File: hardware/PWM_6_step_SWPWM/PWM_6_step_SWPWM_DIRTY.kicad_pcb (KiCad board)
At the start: 2 copper layers, 104.6 x 84.2 mm, 40 parts, among them J1 Conn_01x15, J2 Conn_01x15, J3 Screw_Terminal_01x02, J4 Conn_01x06_Pin, J5 Screw_Terminal_01x03, Q1 IRLZ44N, Q2 IRLZ44N, Q3 IRLZ44N, Q4 IRLZ44N, Q5 IRLZ44N, Q6 IRLZ44N, U1 IR2110, U2 IR2110, U3 IR2110

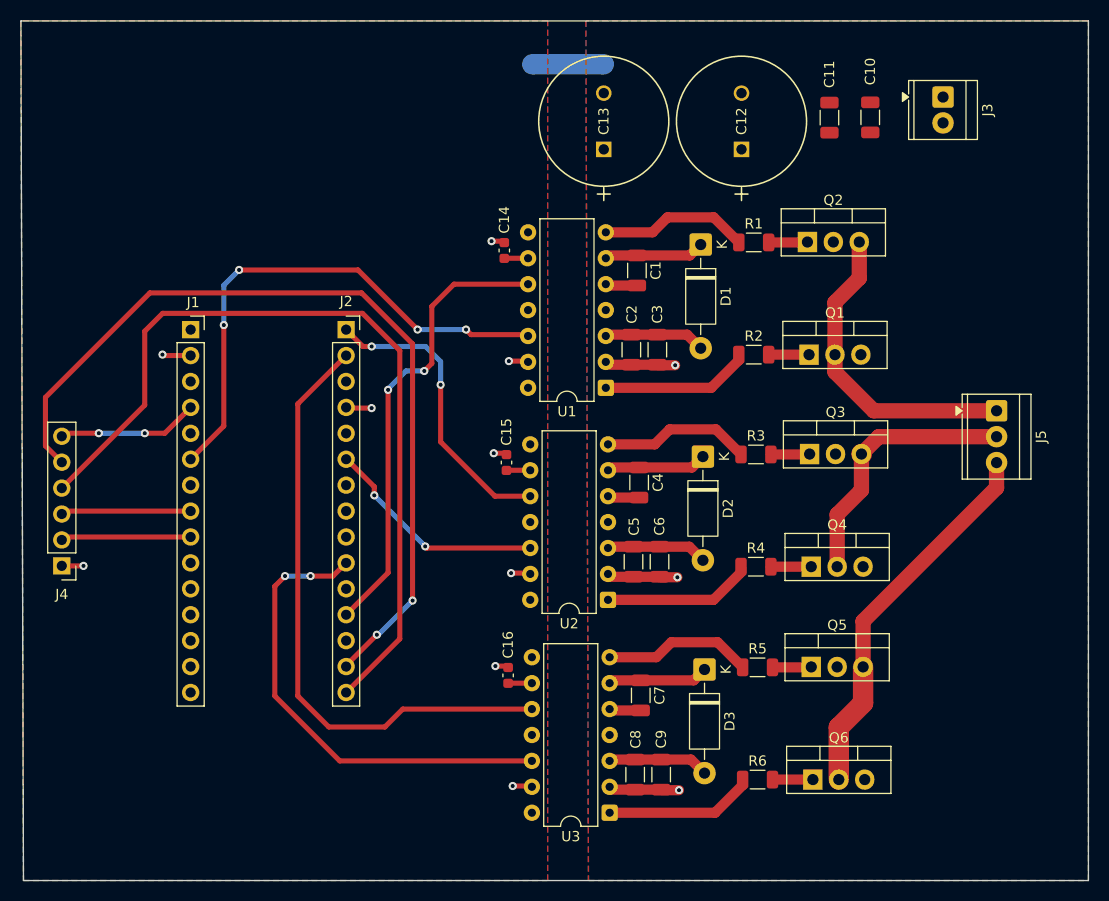
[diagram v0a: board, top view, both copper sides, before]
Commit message: modifications of 6 step pcb after advice taken
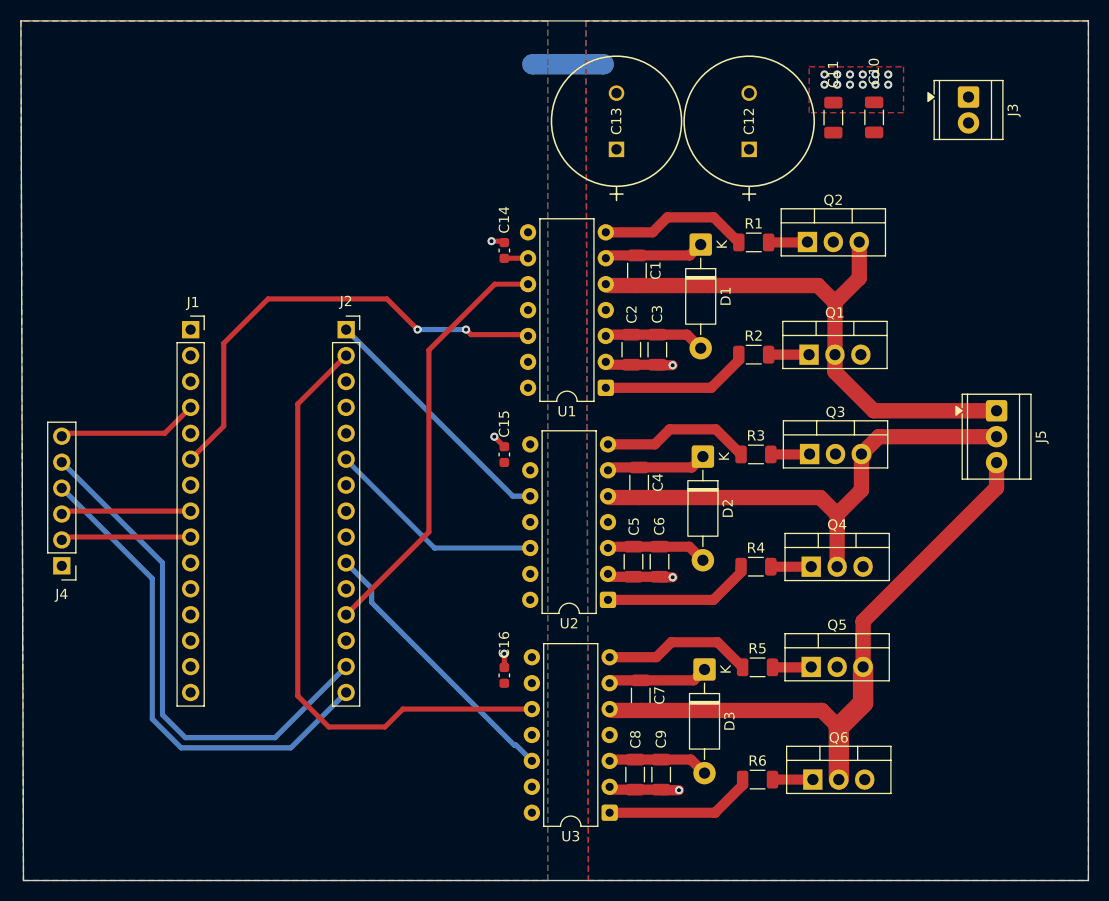
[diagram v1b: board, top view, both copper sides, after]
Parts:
- moved J3 2.50 mm to (222.2, 48.0)
- moved C13 1.25 mm to (187.8, 53.1)
- moved C15 0.81 mm to (176.8, 83.0)
- moved C12 0.75 mm to (200.8, 53.1)
- moved C10 0.38 mm to (213.0, 50.0)
- moved C11 0.38 mm to (209.0, 50.0)
- moved C16 0.38 mm to (176.8, 104.6)
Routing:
- net /MCU/PB4: track 83.7 -> 50.8 mm, vias 2 -> 0
- net /MCU/PB5: track 81.7 -> 48.7 mm
- net /PHASE_C: track 40.6 -> 60.7 mm
- net /PHASE_B: track 29.1 -> 49.2 mm
- net /PHASE_A: track 34.2 -> 54.3 mm
- net /MCU/PF0: track 46.5 -> 27.1 mm, vias 2 -> 0
- net GNDD: track 17.1 -> 4.44 mm, vias 9 -> 3
- net /MCU/PA7: track 51.7 -> 46.0 mm, vias 4 -> 2
- net +3.3V: track 8.03 -> 3.01 mm
- net /MCU/PA9: track 29.6 -> 25.0 mm, vias 2 -> 0
- net /MCU/PA8: track 45.1 -> 41.7 mm, vias 2 -> 0
- net GNDPWR: track 20.8 -> 20.1 mm, vias 3 -> 15
- net /MCU/PB0: track 22.3 -> 21.8 mm, vias 2 -> 0
- net +5V: vias 2 -> 0
- added copper zone on F.Cu, net GNDPWR

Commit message: pcb fixes
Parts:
- moved J5 7.50 mm to (224.8, 86.2)
- moved C15 0.54 mm to (176.5, 82.5)
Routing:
- net /PHASE_C: track 60.7 -> 54.6 mm
- net /PHASE_A: track 54.3 -> 57.0 mm
- net /PHASE_B: track 49.2 -> 51.4 mm
- net GNDPWR: track 20.1 -> 18.9 mm
- net +3.3V: track 3.01 -> 2.34 mm
- net +12V: track 29.7 -> 29.2 mm
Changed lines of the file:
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@@
 	(footprint "TerminalBlock_TE-Connectivity:TerminalBlock_TE_282834-3_1x03_P2.54mm_Horizontal"
 		(layer "F.Cu")
-		(at 225 78.71 -90)
+		(at 224.75 86.21 -90)
 		(descr "Terminal Block TE 282834-3, 3 pins, pitch 2.54mm, size 8.08x6.5mm, drill diameter 1.1mm, pad diameter 2.1mm, http://www.te.com/commerce/DocumentDelivery/DDEController?Action=showdoc&DocId=Customer+Drawing%7F282834%7FC1%7Fpdf%7FEnglish%7FENG_CD_282834_C1.pdf")
 		(tags "THT Terminal Block TE 282834-3 pitch 2.54mm size 8.08x6.5mm drill 1.1mm pad 2.1mm")
@@
 	(footprint "Capacitor_SMD:C_0603_1608Metric"
 		(layer "F.Cu")
-		(at 176.75 83 -90)
+		(at 176.5 82.525 -90)
 		(descr "Capacitor SMD 0603 (1608 Metric), square (rectangular) end terminal, IPC-7351 nominal, (Body size source: IPC-SM-782 page 76, https://www.pcb-3d.com/wordpress/wp-content/uploads/ipc-sm-782a_amendment_1_and_2.pdf)")
 		(tags "capacitor")
@@
 	)
 	(segment
-		(start 189.75 66.435)
-		(end 186.835 66.435)
+		(start 224.75 86.21)
+		(end 220.46 86.21)
 		(width 1.5)
 		(layer "F.Cu")
@@
 	)
 	(segment
-		(start 207.505 66.435)
-		(end 209.16 68.09)
+		(start 189.75 66.435)
+		(end 186.835 66.435)
 		(width 1.5)
 		(layer "F.Cu")
@@
 	)
 	(segment
-		(start 209.16 68.09)
-		(end 209.16 73.21)
+		(start 220.46 86.21)
+		(end 209.16 74.91)
 		(width 1.5)
 		(layer "F.Cu")
@@
 	)
 	(segment
-		(start 209.16 74.91)
-		(end 209.16 73.21)
+		(start 207.505 66.435)
+		(end 209.16 68.09)
 		(width 1.5)
 		(layer "F.Cu")
@@
 	)
 	(segment
-		(start 189.75 66.435)
-		(end 207.505 66.435)
+		(start 209.16 74.91)
+		(end 209.16 73.21)
 		(width 1.5)
 		(layer "F.Cu")
@@
 	)
 	(segment
-		(start 211.54 62.17)
-		(end 211.54 65.71)
+		(start 209.16 68.09)
+		(end 209.16 73.21)
 		(width 1.5)
 		(layer "F.Cu")
@@
 	)
 	(segment
-		(start 186.835 66.435)
-		(end 186.7 66.3)
-		(width 0.25)
-		(layer "F.Cu")
-		(net "/PHASE_A")
-	)
-	(segment
-		(start 212.96 78.71)
-		(end 209.16 74.91)
+		(start 189.75 66.435)
+		(end 207.505 66.435)
 		(width 1.5)
 		(layer "F.Cu")
@@
 	)
 	(segment
-		(start 225 78.71)
-		(end 212.96 78.71)
+		(start 211.54 62.17)
+		(end 211.54 65.71)
 		(width 1.5)
 		(layer "F.Cu")
@@
 	)
 	(segment
-		(start 186.98 74.2)
-		(end 186.7 73.92)
-		(width 0.25)
+		(start 193.875 115.895367)
+		(end 192.175 115.895367)
+		(width 1)
 		(layer "F.Cu")
 		(net "GNDPWR")
@@
 	)
 	(segment
-		(start 187.195 94.981077)
-		(end 186.915 94.701077)
-		(width 0.25)
-		(layer "F.Cu")
-		(net "GNDPWR")
-	)
-	(segment
 		(start 193.25 95.031077)
 		(end 192.015 95.031077)
@@
 	)
 	(segment
-		(start 193.875 115.895367)
-		(end 192.175 115.895367)
-		(width 1)
-		(layer "F.Cu")
-		(net "GNDPWR")
-	)
-	(segment
 		(start 192.015 95.031077)
 		(end 191.965 94.981077)
@@
 	)
 	(segment
-		(start 187.355 115.845367)
-		(end 187.075 115.565367)
-		(width 0.25)
-		(layer "F.Cu")
-		(net "GNDPWR")
-	)
-	(segment
 		(start 192.175 115.895367)
 		(end 192.125 115.845367)
@@
 	)
 	(segment
-		(start 176.615 62.09)
-		(end 176.75 62.225)
+		(start 176.5 81.75)
+		(end 176.5 80.75)
 		(width 0.5)
 		(layer "F.Cu")
@@
 	)
 	(segment
-		(start 179.375 115.485367)
-		(end 179.455 115.565367)
+		(start 176.615 62.09)
+		(end 176.75 62.225)
 		(width 0.5)
 		(layer "F.Cu")
@@
 	)
 	(segment
-		(start 175.775 81.25)
-		(end 176.75 82.225)
+		(start 179.375 115.485367)
+		(end 179.455 115.565367)
 		(width 0.5)
 		(layer "F.Cu")
@@
 	)
 	(via
-		(at 175.775 81.25)
+		(at 176.5 80.75)
 		(size 0.8)
 		(drill 0.4)
@@
 	)
 	(segment
-		(start 177.11 105.405367)
-		(end 176.875 105.170367)
-		(width 0.25)
-		(layer "F.Cu")
-		(net "+3.3V")
-	)
-	(segment
 		(start 179.08 63.76)
 		(end 176.735 63.76)
@@
 	)
 	(segment
-		(start 176.735 63.76)
-		(end 176.5 63.525)
-		(width 0.25)
-		(layer "F.Cu")
-		(net "+3.3V")
-	)
-	(segment
-		(start 187.045 92.031077)
-		(end 186.915 92.161077)
-		(width 0.25)
-		(layer "F.Cu")
-		(net "+12V")
-	)
-	(segment
 		(start 191.965 92.031077)
 		(end 194.885 92.031077)
@@
 	)
 	(segment
-		(start 186.83 71.25)
-		(end 186.7 71.38)
-		(width 0.25)
-		(layer "F.Cu")
-		(net "+12V")
-	)
-	(segment
 		(start 195.045 112.895367)
 		(end 196.375 114.225367)
@@
 	)
 	(segment
-		(start 187.205 112.895367)
-		(end 187.075 113.025367)
-		(width 0.25)
-		(layer "F.Cu")
-		(net "+12V")
-	)
-	(segment
 		(start 194.67 71.25)
 		(end 196 72.58)
@@
 	)
 	(segment
-		(start 186.975 63.485)
-		(end 186.7 63.76)
-		(width 0.25)
-		(layer "F.Cu")
-		(net "Net-(D1-K)")
-	)
-	(segment
 		(start 189.75 63.485)
 		(end 186.975 63.485)
@@
 	)
 	(segment
-		(start 211.915 99.335)
-		(end 225 86.25)
+		(start 221.835 91.29)
+		(end 211.915 101.21)
 		(width 1.5)
 		(layer "F.Cu")
@@
 		(start 209.535 109.735367)
 		(end 209.535 114.855367)
-		(width 2)
+		(width 1.5)
 		(layer "F.Cu")
 		(net "/PHASE_C")
 	)
 	(segment
-		(start 187.21 108.080367)
-		(end 187.075 107.945367)
-		(width 0.25)
+		(start 211.915 103.815367)
+		(end 211.915 107.355367)
+		(width 1.5)
 		(layer "F.Cu")
 		(net "/PHASE_C")
 	)
 	(segment
-		(start 211.915 99.335)
+		(start 211.915 101.21)
 		(end 211.915 103.815367)
 		(width 1.5)
@@
 	)
 	(segment
-		(start 225 86.25)
-		(end 225 83.79)
+		(start 224.75 91.29)
+		(end 221.835 91.29)
 		(width 1.5)
 		(layer "F.Cu")
@@
 	)
 	(segment
-		(start 211.915 103.815367)
-		(end 211.915 107.355367)
-		(width 2)
-		(layer "F.Cu")
-		(net "/PHASE_C")
-	)
-	(segment
 		(start 211.915 107.355367)
 		(end 209.535 109.735367)
-		(width 2)
+		(width 1.5)
 		(layer "F.Cu")
 		(net "/PHASE_C")
@@
 	)
 	(segment
-		(start 187.35 105.130367)
-		(end 187.075 105.405367)
-		(width 0.25)
-		(layer "F.Cu")
-		(net "Net-(D3-K)")
-	)
-	(segment
 		(start 190.125 105.130367)
 		(end 195.31 105.130367)
@@
 	)
 	(segment
-		(start 187.19 84.266077)
-		(end 186.915 84.541077)
-		(width 0.25)
-		(layer "F.Cu")
-		(net "Net-(D2-K)")
-	)
-	(segment
 		(start 189.965 84.266077)
 		(end 195.15 84.266077)
@@
 	)
 	(segment
-		(start 213.456077 81.25)
-		(end 225 81.25)
+		(start 191.498923 88.75)
+		(end 211 88.75)
 		(width 1.5)
 		(layer "F.Cu")
@@
 	)
 	(segment
-		(start 189.965 87.216077)
-		(end 207.72 87.216077)
+		(start 186.915 87.081077)
+		(end 189.83 87.081077)
 		(width 1.5)
 		(layer "F.Cu")
@@
 	)
 	(segment
-		(start 187.05 87.216077)
-		(end 186.915 87.081077)
-		(width 0.25)
+		(start 211.755 85.505)
+		(end 215 88.75)
+		(width 1.5)
 		(layer "F.Cu")
 		(net "/PHASE_B")
 	)
 	(segment
-		(start 207.72 87.216077)
-		(end 209.375 88.871077)
+		(start 209.375 90.375)
+		(end 209.375 93.991077)
 		(width 1.5)
 		(layer "F.Cu")
@@
 	)
 	(segment
-		(start 211.755 86.491077)
-		(end 209.375 88.871077)
+		(start 211 88.75)
+		(end 209.375 90.375)
 		(width 1.5)
 		(layer "F.Cu")
@@
 	)
 	(segment
-		(start 189.965 87.216077)
-		(end 187.05 87.216077)
+		(start 211.755 82.951077)
+		(end 211.755 85.505)
 		(width 1.5)
 		(layer "F.Cu")
@@
 	)
 	(segment
-		(start 211.755 82.951077)
-		(end 211.755 86.491077)
+		(start 189.965 87.216077)
+		(end 191.498923 88.75)
 		(width 1.5)
 		(layer "F.Cu")
@@
 	)
 	(segment
-		(start 209.375 88.871077)
-		(end 209.375 93.991077)
+		(start 215 88.75)
+		(end 211 88.75)
 		(width 1.5)
 		(layer "F.Cu")
@@
 	)
 	(segment
-		(start 213.456077 81.25)
-		(end 211.755 82.951077)
+		(start 224.75 88.75)
+		(end 215 88.75)
 		(width 1.5)
 		(layer "F.Cu")
@@
 	)
 	(segment
-		(start 206.42 62.21)
-		(end 206.46 62.17)
-		(width 0.25)
-		(layer "F.Cu")
-		(net "Net-(Q2-G)")
-	)
-	(segment
 		(start 202.8775 82.991077)
 		(end 206.635 82.991077)
@@
 	)
 	(segment
-		(start 206.795 103.855367)
-		(end 206.835 103.815367)
-		(width 0.25)
-		(layer "F.Cu")
-		(net "Net-(Q5-G)")
-	)
-	(segment

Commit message: fixes to PCB
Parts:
- moved C10 1.19 mm to (213.9, 50.8)
- moved C11 1.15 mm to (209.9, 50.7)
- moved C16 0.92 mm to (176.8, 103.7)
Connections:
- J1 pad 7: /MCU/PA6 -> GNDD
- U1 pad 11: /Gate_Driver_A/SD -> GNDD
- U2 pad 11: /Gate_Driver_B/SD -> GNDD
- U3 pad 11: /Gate_Driver_C/SD -> GNDD
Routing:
- net /MCU/PF0: track 27.1 -> 32.2 mm
- net /MCU/PB5: track 48.7 -> 51.8 mm
- net /MCU/PA7: track 46.0 -> 44.5 mm, vias 2 -> 0
